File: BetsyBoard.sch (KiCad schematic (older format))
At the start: 46 parts, among them CON1 SDMMC_Card, P1 USB_OTG, P2 Analog, P3 Digital, P4 JLINK-SWD, P5 POWER, P6 CORTEX-JTAG, P7 PG, SW1 SW_PUSH, U1 STM32L486Rx-LQFP64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

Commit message: VBAT stuff
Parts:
- added P8: POWER, w_conn_jst-ph:s2b-ph-sm4-tb, symbol CONN_01X02
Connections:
- wire segments 129 -> 131
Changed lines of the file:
@@
 LIBS:valves
 LIBS:engstad
+LIBS:BetsyBoard-cache
 EELAYER 25 0
 EELAYER END
@@
 Text Label 4650 1200 0    60   ~ 0
 FB
-Text Label 4250 2800 2    60   ~ 0
+Text Label 4500 2800 2    60   ~ 0
 VBAT
 Text Label 8550 4000 0    60   ~ 0
 OTG_5V
+$Comp
+L CONN_01X02 P8
+U 1 1 56691320
+P 4050 2850
+F 0 "P8" H 4050 3000 50  0000 C CNN
+F 1 "POWER" V 4150 2850 50  0000 C CNN
+F 2 "w_conn_jst-ph:s2b-ph-sm4-tb" H 4050 2850 60  0001 C CNN
+F 3 "" H 4050 2850 60  0000 C CNN
+	1    4050 2850
+	-1   0    0    -1
+$EndComp
+$Comp
+L GND #PWR030
+U 1 1 5669151A
+P 4400 3150
+F 0 "#PWR030" H 4400 2900 50  0001 C CNN
+F 1 "GND" H 4400 3000 50  0000 C CNN
+F 2 "" H 4400 3150 60  0000 C CNN
+F 3 "" H 4400 3150 60  0000 C CNN
+	1    4400 3150
+	1    0    0    -1
+$EndComp
+Wire Wire Line
+	4250 2900 4400 2900
+Wire Wire Line
+	4400 2900 4400 3150
 $EndSCHEMATC

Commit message: Work towards v0.5
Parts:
- removed C14: 1nF, smd:SM0603, symbol C
- removed JP1: JUMPER3, xess:xess-JP2, symbol JUMPER3
- removed P5: POWER, engstad:pin-socket-2, symbol CONN_01X02
- removed R6: 1M, smd:SM0603, symbol R
- removed SW1: SW_PUSH, engstad:tactile-switch-te-147873-2, symbol SW_PUSH
- removed U2: TPS63051, engstad:dsbga-12, symbol TPS63051
- removed U4: PUSBM5V5X4, engstad:dfn1616-6, symbol PUSBMxX4
- added C14: 0.1uF, smd:SM0603, symbol C_Small
- added L4: Bead, smd:SM0805, symbol L_Small
- added P5: VIN, engstad:pin-strip-1, symbol CONN_01X01
- added R6: 10.0k, smd:SM0603, symbol R_Small
- added R7: 10k, smd:SM0603, symbol R
- added R8: 0, smd:SM0603, symbol R_Small
- added SW1: RST, engstad:tactile-switch-te-147873-2, symbol SW_PUSH_NO
- added U2: RClamp0504S, w_smd_trans:sot23-6, symbol RClamp0504S
- added U4: TPS56x200, w_smd_trans:sot23-6, symbol TPS56x200
- C11: value 10uF -> 22uF
- C12, C13: footprint smd:SM1206 -> smd:SM0805
- L1: value 1.5uH -> 2.2uH
- L2: footprint w_smd_cap:c_1210 -> smd:SM0603
- P2, P3: footprint w_pin_strip:pin_strip_16 -> engstad:pin-strip-16
- P4: footprint w_pin_strip:pin_strip_6 -> engstad:pin-strip-6
- P7: value PG -> RTC; footprint xess:HDR_1x1 -> engstad:pin-strip-1
- P8: value POWER -> BATT; footprint w_conn_jst-ph:s2b-ph-sm4-tb -> engstad:pin-socket-2
- R1: value 560k -> 33.2k
- R2: value 180k -> 10k
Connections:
- net labels added: OSC_IN, OSC_OUT, SW, VDDSD
- net labels removed: +3.3VADC, PG, PVD, VDD_SD, VUSB
- wire segments 131 -> 115
- no-connect marks 2 -> 3
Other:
- note added: "DNP"
- moved on the sheet: C1, C10, C11, C12, C13, C15, C16, C17, C18, C19, C2, C3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

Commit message: Trying to fit DIP switch
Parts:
- removed R7: 10k, smd:SM0603, symbol R
- removed R8: 0, smd:SM0603, symbol R_Small
- added D2: BAV170, w_smd_trans:sot23, symbol D_Schottky_x2_KCom_AKA
- added SW2: spdp-2x, engstad:slide-switch-smd-cas-220-d20, symbol spdp-2x
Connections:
- wire segments 115 -> 122
- no-connect marks 3 -> 4
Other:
- note removed: "DNP"
- moved on the sheet: C18, P8, R4

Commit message: A little more work
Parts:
- removed D2: BAV170, w_smd_trans:sot23, symbol D_Schottky_x2_KCom_AKA
- removed unit 1 of SW2
- added unit 2 of SW2
- P7: footprint engstad:pin-strip-1 -> engstad:pin-socket-1
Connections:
- wire segments 122 -> 121
- no-connect marks 4 -> 3
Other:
- moved on the sheet: C18, P8, U4

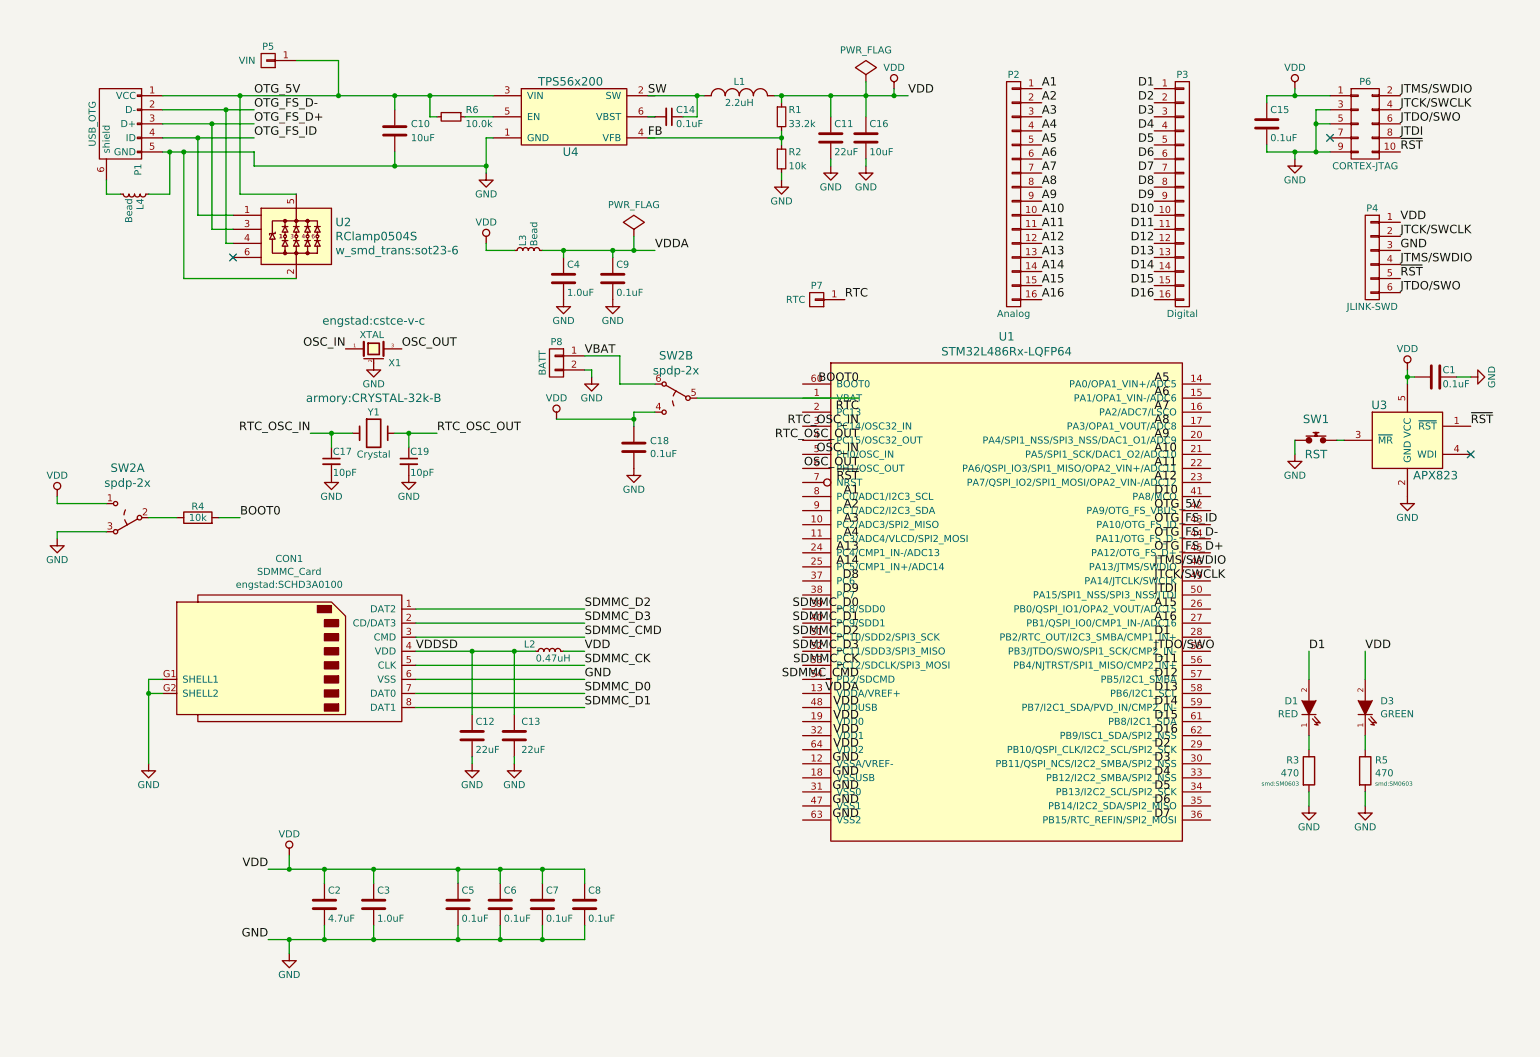
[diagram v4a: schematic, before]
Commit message: Move connection from NRST to /MR.
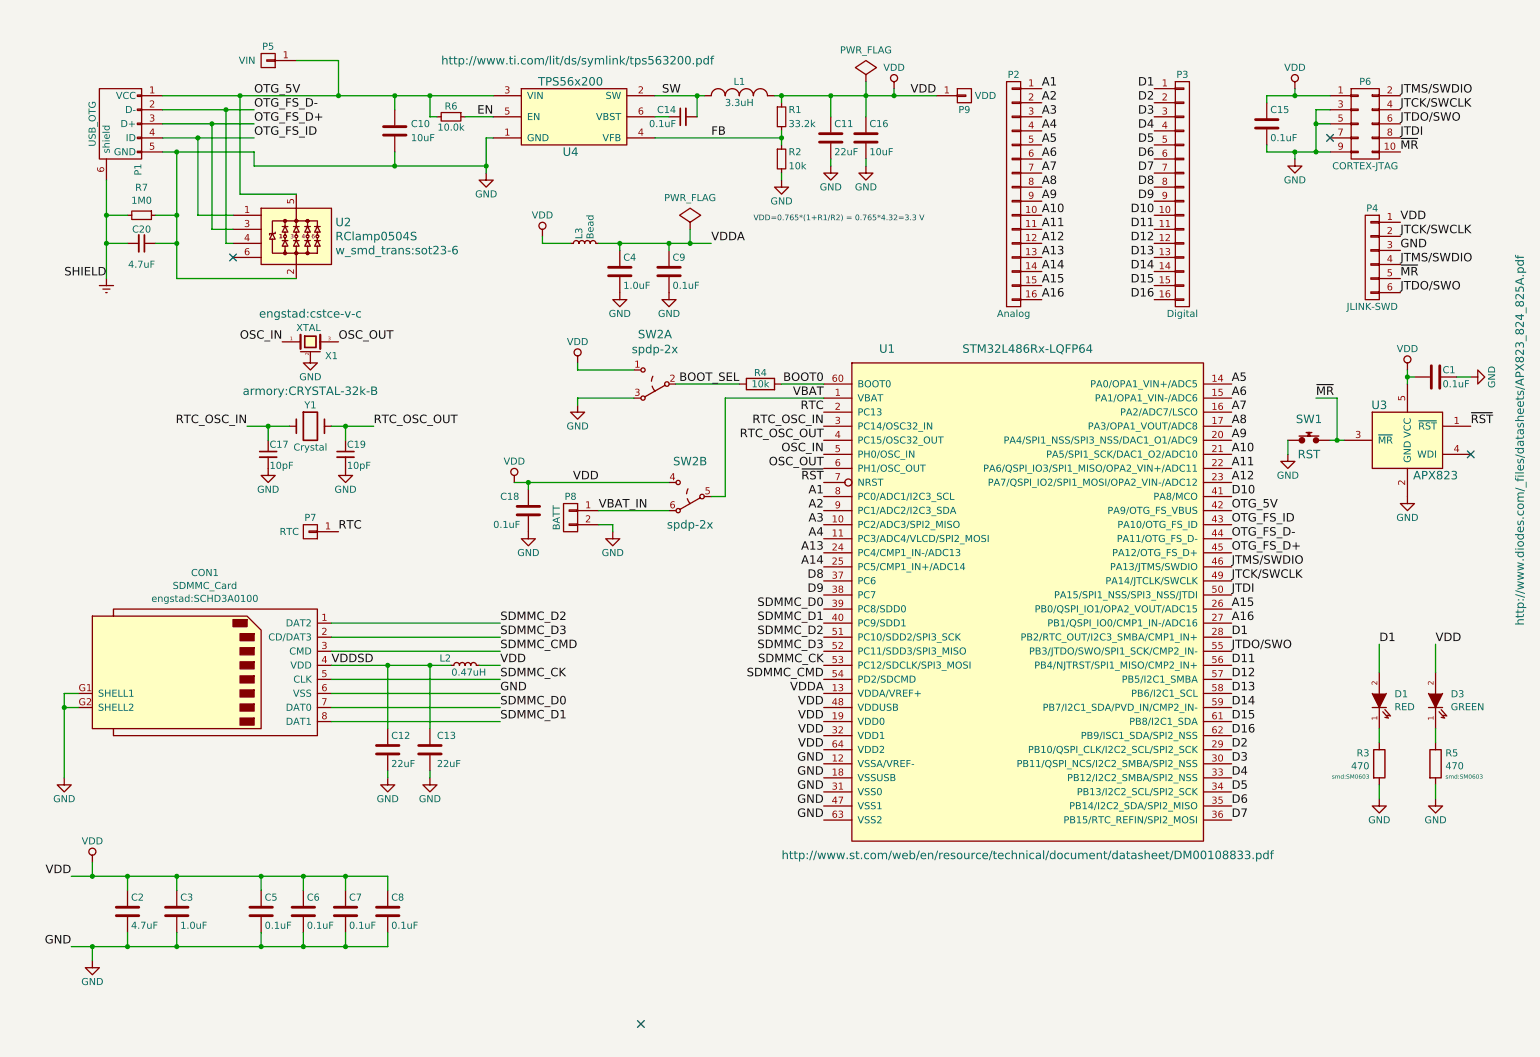
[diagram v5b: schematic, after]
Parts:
- removed L4: Bead, smd:SM0805, symbol L_Small
- added C20: 4.7uF, smd:SM0603, symbol C_Small
- added P9: VDD, engstad:pin-strip-1, symbol CONN_01X01
- added R7: 1M0, smd:SM0603, symbol R_Small
- D1, D3: footprint LEDs:LED-0805 -> w_smd_leds:Led_0603
- L1: value 2.2uH -> 3.3uH
- P1: footprint engstad:usb-otg-short -> engstad:usb-micro-b-amphenol-fci-10118194
- SW1: footprint engstad:tactile-switch-te-147873-2 -> engstad:tactile-switch-evpay-34x29mm
- SW2: footprint (none) -> engstad:slide-switch-smd-cas-220-d20
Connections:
- net A1: now also U1.8 (PC0/ADC1/I2C3_SCL)
- net A10: now also U1.21 (PA5/SPI1_SCK/DAC1_O2/ADC10)
- net A11: now also U1.22 (PA6/QSPI_IO3/SPI1_MISO/OPA2_VIN+/ADC11)
- net A12: now also U1.23 (PA7/QSPI_IO2/SPI1_MOSI/OPA2_VIN-/ADC12)
- net A13: now also U1.24 (PC4/CMP1_IN-/ADC13)
- net A14: now also U1.25 (PC5/CMP1_IN+/ADC14)
- net A15: now also U1.26 (PB0/QSPI_IO1/OPA2_VOUT/ADC15)
- net A16: now also U1.27 (PB1/QSPI_IO0/CMP1_IN-/ADC16)
- net A2: now also U1.9 (PC1/ADC2/I2C3_SDA)
- net A3: now also U1.10 (PC2/ADC3/SPI2_MISO)
- net A4: now also U1.11 (PC3/ADC4/VLCD/SPI2_MOSI)
- net A5: now also U1.14 (PA0/OPA1_VIN+/ADC5)
- net A6: now also U1.15 (PA1/OPA1_VIN-/ADC6)
- net A7: now also U1.16 (PA2/ADC7/LSCO)
- net A8: now also U1.17 (PA3/OPA1_VOUT/ADC8)
- net A9: now also U1.20 (PA4/SPI1_NSS/SPI3_NSS/DAC1_O1/ADC9)
- net BOOT0: now also U1.60 (BOOT0)
- net D1: now also U1.28 (PB2/RTC_OUT/I2C3_SMBA/CMP1_IN+)
- net D10: now also U1.41 (PA8/MCO)
- net D11: now also U1.56 (PB4/NJTRST/SPI1_MISO/CMP2_IN+)
- net D12: now also U1.57 (PB5/I2C1_SMBA)
- net D13: now also U1.58 (PB6/I2C1_SCL)
- net D14: now also U1.59 (PB7/I2C1_SDA/PVD_IN/CMP2_IN-)
- net D15: now also U1.61 (PB8/I2C1_SDA)
- net D16: now also U1.62 (PB9/ISC1_SDA/SPI2_NSS)
- net D2: now also U1.29 (PB10/QSPI_CLK/I2C2_SCL/SPI2_SCK)
- net D3: now also U1.30 (PB11/QSPI_NCS/I2C2_SMBA/SPI2_NSS)
- net D4: now also U1.33 (PB12/I2C2_SMBA/SPI2_NSS)
- net D5: now also U1.34 (PB13/I2C2_SCL/SPI2_SCK)
- net D6: now also U1.35 (PB14/I2C2_SDA/SPI2_MISO)
- net D7: now also U1.36 (PB15/RTC_REFIN/SPI2_MOSI)
- net D8: now also U1.37 (PC6)
- net D9: now also U1.38 (PC7)
- net FB: now also U4.4 (VFB)
- net GND: now also U1.12 (VSSA/VREF-), U1.18 (VSSUSB), U1.31 (VSS0), U1.47 (VSS1), U1.63 (VSS2), C20.1, R7.1
- net JTCK/SWCLK: now also U1.49 (PA14/JTCLK/SWCLK)
- net JTDI: now also U1.50 (PA15/SPI1_NSS/SPI3_NSS/JTDI)
- net JTDO/SWO: now also U1.55 (PB3/JTDO/SWO/SPI1_SCK/CMP2_IN-)
- net JTMS/SWDIO: now also U1.46 (PA13/JTMS/SWDIO)
- net OSC_IN: now also U1.5 (PH0/OSC_IN)
- net OSC_OUT: now also U1.6 (PH1/OSC_OUT)
- net OTG_5V: now also U1.42 (PA9/OTG_FS_VBUS)
- net OTG_FS_D+: now also U1.45 (PA12/OTG_FS_D+)
- net OTG_FS_D-: now also U1.44 (PA11/OTG_FS_D-)
- net OTG_FS_ID: now also U1.43 (PA10/OTG_FS_ID)
- net RTC: now also U1.2 (PC13)
- net RTC_OSC_IN: now also U1.3 (PC14/OSC32_IN)
- net RTC_OSC_OUT: now also U1.4 (PC15/OSC32_OUT)
- net SDMMC_CK: now also U1.53 (PC12/SDCLK/SPI3_MOSI)
- net SDMMC_CMD: now also U1.54 (PD2/SDCMD)
- net SDMMC_D0: now also U1.39 (PC8/SDD0)
- net SDMMC_D1: now also U1.40 (PC9/SDD1)
- net SDMMC_D2: now also U1.51 (PC10/SDD2/SPI3_SCK)
- net SDMMC_D3: now also U1.52 (PC11/SDD3/SPI3_MISO)
- net SW: now also C14.2, U4.2 (SW); no longer C14.1
- net VBAT: now also SW2.5, U1.1 (VBAT); no longer P8.1 (P1), SW2.6
- net VDD: now also U1.19 (VDD0), U1.32 (VDD1), U1.48 (VDDUSB), U1.64 (VDD2), P9.1 (P1)
- net VDDA: now also U1.13 (VDDA/VREF+)
- net ~RST: now also U1.7 (NRST); no longer P4.5 (P5), P6.10 (P10)
- net Earth: now reaches P1.6 (shield)
- net Earth: now also C20.2, R7.2
- net BOOT_SEL: now reaches R4.1, SW2.2
- net ~MR: now reaches SW1.2, U3.3 (~MR~)
- net ~MR: now also P4.5 (P5), P6.10 (P10)
- net EN: now reaches R6.1, U4.5 (EN)
- net at U4.6 (VBST): now also C14.1; no longer C14.2
- new net VBAT_IN: P8.1 (P1), SW2.6
- no-connect marks 3 -> 4
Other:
- note added: "VDD=0.765*(1+R1/R2) = 0.765*4.32=3.3 V\n"
- moved on the sheet: C12, C13, C14, C17, C18, C19, C2, C3, C4, C5, C6, C7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

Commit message: Adding more pin numbers on silkscreen.
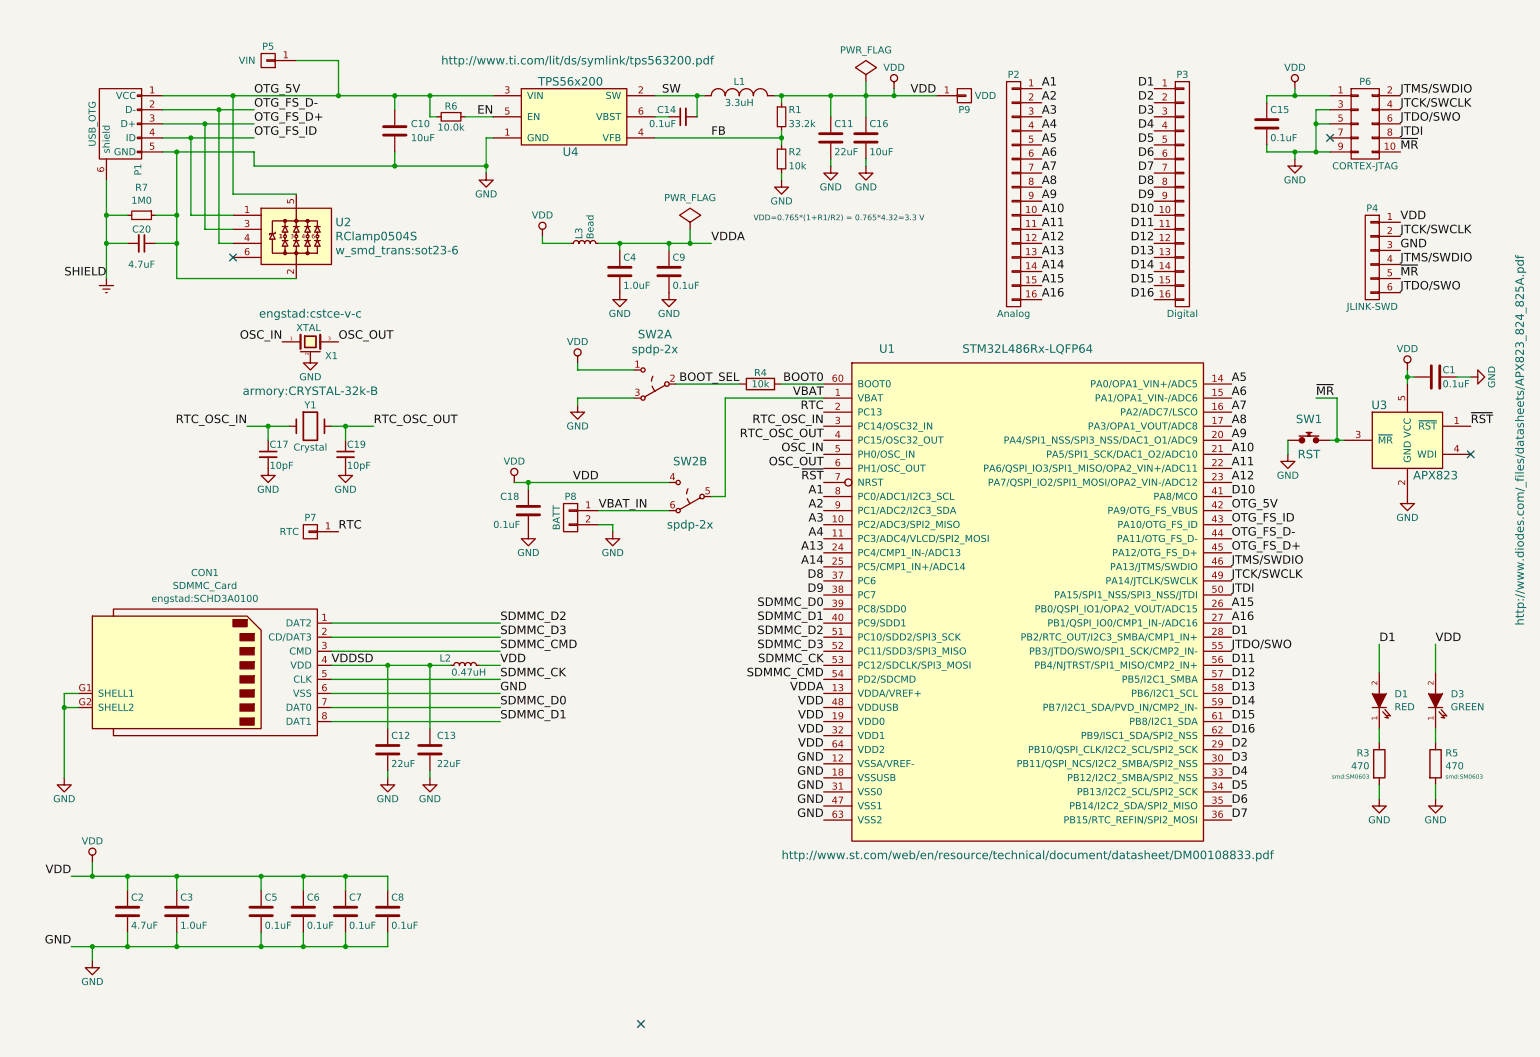
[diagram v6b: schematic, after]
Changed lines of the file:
@@
 RTC
 Wire Wire Line
-	850  6600 3100 6600
+	850  6600 1000 6600
+Wire Wire Line
+	1000 6600 1250 6600
+Wire Wire Line
+	1250 6600 1600 6600
+Wire Wire Line
+	1600 6600 2200 6600
+Wire Wire Line
+	2200 6600 2500 6600
+Wire Wire Line
+	2500 6600 2800 6600
+Wire Wire Line
+	2800 6600 3100 6600
 Wire Wire Line
 	1250 6600 1250 6700
@@
 	1250 7100 1250 7000
 Wire Wire Line
-	850  7100 3100 7100
+	850  7100 1000 7100
+Wire Wire Line
+	1000 7100 1250 7100
+Wire Wire Line
+	1250 7100 1600 7100
+Wire Wire Line
+	1600 7100 2200 7100
+Wire Wire Line
+	2200 7100 2500 7100
+Wire Wire Line
+	2500 7100 2800 7100
+Wire Wire Line
+	2800 7100 3100 7100
 Wire Wire Line
 	1600 7100 1600 7000
@@
 Connection ~ 1000 7100
 Wire Wire Line
-	1500 1150 2150 1150
-Wire Wire Line
-	1500 1250 2150 1250
-Wire Wire Line
-	1500 1350 2150 1350
-Wire Wire Line
-	1500 1050 3850 1050
+	1500 1150 1900 1150
+Wire Wire Line
+	1900 1150 2150 1150
+Wire Wire Line
+	1500 1250 1800 1250
+Wire Wire Line
+	1800 1250 2150 1250
+Wire Wire Line
+	1500 1350 1700 1350
+Wire Wire Line
+	1700 1350 2150 1350
+Wire Wire Line
+	1500 1050 2000 1050
+Wire Wire Line
+	2000 1050 2750 1050
+Wire Wire Line
+	2750 1050 3150 1050
+Wire Wire Line
+	3150 1050 3400 1050
+Wire Wire Line
+	3400 1050 3850 1050
 Text Label 2150 1050 0    60   ~ 0
 OTG_5V
@@
 D1
 Wire Wire Line
-	2700 5100 3550 5100
+	2700 5100 3100 5100
+Wire Wire Line
+	3100 5100 3400 5100
+Wire Wire Line
+	3400 5100 3550 5100
 $Comp
 L C C12
@@
 $EndComp
 Wire Wire Line
-	4600 2100 5400 2100
+	4600 2100 4750 2100
+Wire Wire Line
+	4750 2100 5100 2100
+Wire Wire Line
+	5100 2100 5250 2100
+Wire Wire Line
+	5250 2100 5400 2100
 Wire Wire Line
 	4750 2100 4750 2150
@@
 JTMS/SWDIO
 Wire Wire Line
-	1950 1150 1950 2100
-Connection ~ 1950 1150
-Wire Wire Line
-	1850 1250 1850 2000
-Wire Wire Line
-	1850 2000 2000 2000
-Connection ~ 1850 1250
-Wire Wire Line
-	1750 1350 1750 1900
-Connection ~ 1750 1350
-Wire Wire Line
-	1500 1450 2150 1450
-Wire Wire Line
-	2450 1750 2050 1750
-Connection ~ 2050 1050
-Wire Wire Line
-	2050 1750 2050 1050
+	1900 1150 1900 2100
+Connection ~ 1900 1150
+Wire Wire Line
+	1800 1250 1800 2000
+Wire Wire Line
+	1800 2000 2000 2000
+Connection ~ 1800 1250
+Wire Wire Line
+	1700 1350 1700 1900
+Connection ~ 1700 1350
+Wire Wire Line
+	1500 1450 1600 1450
+Wire Wire Line
+	1600 1450 2150 1450
+Wire Wire Line
+	2450 1750 2000 1750
+Connection ~ 2000 1050
+Wire Wire Line
+	2000 1750 2000 1050
 Wire Wire Line
 	2150 1450 2150 1550
@@
 	2250 3500 2250 3400
 Wire Wire Line
-	2100 3400 2400 3400
-Wire Wire Line
-	2700 3400 3000 3400
+	2100 3400 2250 3400
+Wire Wire Line
+	2250 3400 2400 3400
+Wire Wire Line
+	2700 3400 2800 3400
+Wire Wire Line
+	2800 3400 3000 3400
 Wire Wire Line
 	2800 3400 2800 3500
@@
 $EndComp
 Wire Wire Line
-	10350 3000 10350 3100
+	10350 3000 10350 3050
+Wire Wire Line
+	10350 3050 10350 3100
 NoConn ~ 10800 3600
 $Comp
@@
 $EndComp
 Wire Wire Line
-	5000 1050 5350 1050
+	5000 1050 5300 1050
+Wire Wire Line
+	5300 1050 5350 1050
 $Comp
 L C C16
@@
 	5900 1050 5900 1100
 Wire Wire Line
-	5900 1300 5900 1400
+	5900 1300 5900 1350
+Wire Wire Line
+	5900 1350 5900 1400
 $Comp
 L R_Small R2
@@
 	9800 1150 9700 1150
 Wire Wire Line
-	9700 1150 9700 1450
+	9700 1150 9700 1250
+Wire Wire Line
+	9700 1250 9700 1450
 Wire Wire Line
 	9700 1250 9800 1250
 Wire Wire Line
-	9350 1450 9800 1450
+	9350 1450 9550 1450
+Wire Wire Line
+	9550 1450 9700 1450
+Wire Wire Line
+	9700 1450 9800 1450
 Connection ~ 9700 1250
 Wire Wire Line
@@
 $EndComp
 Wire Wire Line
-	5850 1050 7000 1050
-Wire Wire Line
-	6500 950  6500 1200
+	5850 1050 5900 1050
+Wire Wire Line
+	5900 1050 6250 1050
+Wire Wire Line
+	6250 1050 6500 1050
+Wire Wire Line
+	6500 1050 6700 1050
+Wire Wire Line
+	6700 1050 7000 1050
+Wire Wire Line
+	6500 950  6500 1050
+Wire Wire Line
+	6500 1050 6500 1200
 Connection ~ 6700 1050
 Wire Wire Line
@@
 Connection ~ 3400 1050
 Wire Wire Line
-	1600 1450 1600 2350
+	1600 1450 1600 1900
+Wire Wire Line
+	1600 1900 1600 2100
+Wire Wire Line
+	1600 2100 1600 2350
 Connection ~ 1600 1450
 $Comp
@@
 Connection ~ 1000 6600
 Wire Wire Line
-	3800 1350 3800 1600
+	3800 1350 3800 1550
+Wire Wire Line
+	3800 1550 3800 1600
 Wire Wire Line
 	5300 1050 5300 1200
 Connection ~ 5300 1050
 Wire Wire Line
-	2150 1550 3800 1550
+	2150 1550 3150 1550
+Wire Wire Line
+	3150 1550 3800 1550
 Wire Wire Line
 	3150 1450 3150 1550
@@
 	2700 5300 3900 5300
 Wire Wire Line
-	4000 3800 5100 3800
+	4000 3800 4100 3800
+Wire Wire Line
+	4100 3800 5100 3800
 Wire Wire Line
 	4100 3800 4100 3850
@@
 $EndComp
 Wire Wire Line
-	9350 1050 9800 1050
+	9350 1050 9550 1050
+Wire Wire Line
+	9550 1050 9800 1050
 Wire Wire Line
 	9550 1000 9550 1050
@@
 	900  5300 800  5300
 Wire Wire Line
-	800  5300 800  5900
+	800  5300 800  5400
+Wire Wire Line
+	800  5400 800  5900
 Wire Wire Line
 	800  5400 900  5400
@@
 	10700 3050 10800 3050
 Wire Wire Line
-	1750 1900 2000 1900
-Wire Wire Line
-	1950 2100 2000 2100
+	1700 1900 2000 1900
+Wire Wire Line
+	1900 2100 2000 2100
 Text Label 5050 1050 0    60   ~ 0
 SW
@@
 	6500 1500 6500 1550
 Wire Wire Line
-	9800 3500 9900 3500
+	9800 3500 9850 3500
+Wire Wire Line
+	9850 3500 9900 3500
 Wire Wire Line
 	5100 1200 5000 1200
@@
 Connection ~ 1600 2100
 Wire Wire Line
-	1100 1650 1100 2350
+	1100 1650 1100 1900
+Wire Wire Line
+	1100 1900 1100 2100
+Wire Wire Line
+	1100 2100 1100 2350
 $Comp
 L CONN_01X01 P9
